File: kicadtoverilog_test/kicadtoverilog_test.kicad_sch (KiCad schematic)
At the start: 3 parts, among them X1 DGOF5S3

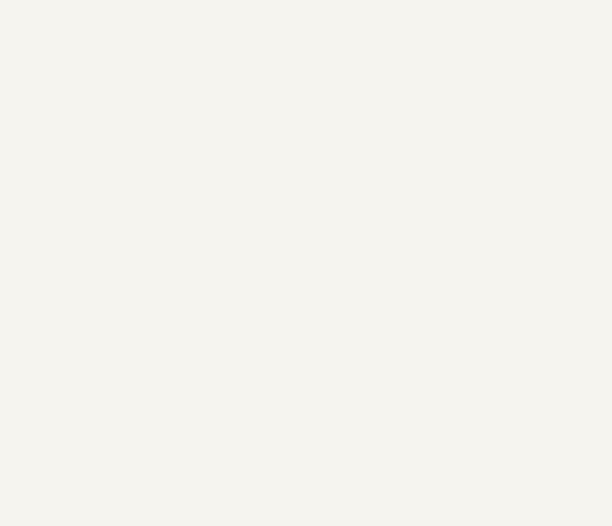
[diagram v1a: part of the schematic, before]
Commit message: Switch to KiCad 6.0 release
Use Command line args with argparse
Add some docs
Copy over synthesis_defs.v to verilog directory during run
Regularize logging
Fix bug with single nets on two module pins (Use wire statements for all nets, with assign statements for each module pin.)
Add test block with big divby3 from Atari TIA chip
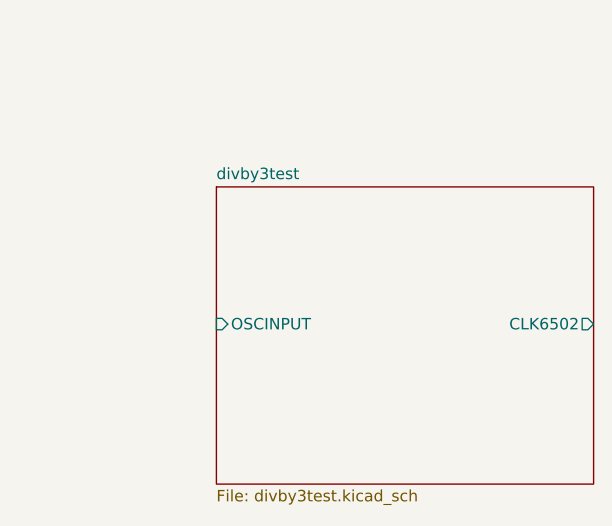
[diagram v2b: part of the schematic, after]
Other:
- added sheet divby3test (divby3test.kicad_sch)
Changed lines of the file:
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@@
 (kicad_sch (version 20211123) (generator eeschema)
-  (paper "A4")
+  (paper "USLetter")
   (wire (pts (xy 114.3 57.15) (xy 114.3 58.42))
     (stroke (width 0) (type default) (color 0 0 0 0))
@@
     (pin "1")
     (pin "2")
+  )
+  (sheet (at 96.52 106.68) (size 41.91 33.02) (fields_autoplaced)
+    (stroke (width 0.1524) (type solid) (color 0 0 0 0))
+    (fill (color 0 0 0 0.0000))
+    (property "Sheet name" "divby3test" (id 0) (at 96.52 105.9684 0)
+      (effects (font (size 1.27 1.27)) (justify left bottom))
+    )
+    (property "Sheet file" "divby3test.kicad_sch" (id 1) (at 96.52 140.2846 0)
+      (effects (font (size 1.27 1.27)) (justify left top))
+    )
+    (pin "CLK6502" output (at 138.43 121.92 0)
+      (effects (font (size 1.27 1.27)) (justify right))
+    )
+    (pin "OSCINPUT" input (at 96.52 121.92 180)
+      (effects (font (size 1.27 1.27)) (justify left))
+    )
   )
   (sheet (at 67.31 49.53) (size 25.4 27.94) (fields_autoplaced)
@@
     (path "/4f2d6a8d-0e80-4d54-bbae-408c1fcd4a62/633f75c5-3e59-4c5c-acaa-7b07045091db" (page "3"))
     (path "/4f2d6a8d-0e80-4d54-bbae-408c1fcd4a62/f15199f8-d839-4b26-a88d-cbb37c25a286" (page "4"))
+    (path "/1ee9928d-39f3-49de-bfea-81da4b94202b" (page "5"))
   )
   (symbol_instances
@@
       (reference "U4") (unit 1) (value "NOT") (footprint "")
     )
+    (path "/1ee9928d-39f3-49de-bfea-81da4b94202b/de77cc3b-6461-4584-bece-1b82a64083cf"
+      (reference "U5") (unit 1) (value "NOR2") (footprint "")
+    )
+    (path "/1ee9928d-39f3-49de-bfea-81da4b94202b/7a863598-1fe4-4965-ab0e-1f5f7c693cce"
+      (reference "U6") (unit 1) (value "NOR2") (footprint "")
+    )
+    (path "/1ee9928d-39f3-49de-bfea-81da4b94202b/aa8b3dd5-a5db-4d28-9f06-c334420f0ab0"
+      (reference "U7") (unit 1) (value "NOR2") (footprint "")
+    )
+    (path "/1ee9928d-39f3-49de-bfea-81da4b94202b/067be3a4-5e77-4472-9815-f50aab9fa6e2"
+      (reference "U8") (unit 1) (value "NOR2") (footprint "")
+    )
+    (path "/1ee9928d-39f3-49de-bfea-81da4b94202b/2800f70a-c288-469b-9829-771526ce2d9e"
+      (reference "U9") (unit 1) (value "NOR2") (footprint "")
+    )
+    (path "/1ee9928d-39f3-49de-bfea-81da4b94202b/cd372e86-2860-41ec-9d38-36aaf34b5770"
+      (reference "U10") (unit 1) (value "AND2") (footprint "")
+    )
+    (path "/1ee9928d-39f3-49de-bfea-81da4b94202b/b0d9aeee-3dba-4aa3-a75e-a4ba0c4a286b"
+      (reference "U11") (unit 1) (value "AND2") (footprint "")
+    )
+    (path "/1ee9928d-39f3-49de-bfea-81da4b94202b/887bada7-fc95-4e33-a94c-ef38c1958dfe"
+      (reference "U12") (unit 1) (value "NOR2") (footprint "")
+    )
+    (path "/1ee9928d-39f3-49de-bfea-81da4b94202b/856303fa-24c8-41cb-88b2-1f106ae8656c"
+      (reference "U13") (unit 1) (value "NOR2") (footprint "")
+    )
+    (path "/1ee9928d-39f3-49de-bfea-81da4b94202b/20582dd1-49d6-455e-9246-f48e6caa6db7"
+      (reference "U14") (unit 1) (value "NOR2") (footprint "")
+    )
+    (path "/1ee9928d-39f3-49de-bfea-81da4b94202b/b4166ee3-09bf-48a7-8d74-8969bd6d2dd3"
+      (reference "U15") (unit 1) (value "NOT") (footprint "")
+    )
+    (path "/1ee9928d-39f3-49de-bfea-81da4b94202b/6c620b1f-3b68-45a2-afba-bbd859b22d82"
+      (reference "U16") (unit 1) (value "NOR2") (footprint "")
+    )
+    (path "/1ee9928d-39f3-49de-bfea-81da4b94202b/d6840884-81c4-4835-9a07-0471b17aca9d"
+      (reference "U17") (unit 1) (value "NOR2") (footprint "")
+    )
+    (path "/1ee9928d-39f3-49de-bfea-81da4b94202b/02ecf064-5973-4753-9e25-8af2823609b1"
+      (reference "U18") (unit 1) (value "NOR2") (footprint "")
+    )
+    (path "/1ee9928d-39f3-49de-bfea-81da4b94202b/3af2825f-8ffc-4a6a-be03-a0adf47385f2"
+      (reference "U19") (unit 1) (value "NOR2") (footprint "")
+    )
+    (path "/1ee9928d-39f3-49de-bfea-81da4b94202b/5f9c655e-4dae-40a5-ae38-5294b8242232"
+      (reference "U20") (unit 1) (value "AND2") (footprint "")
+    )
+    (path "/1ee9928d-39f3-49de-bfea-81da4b94202b/9912dfed-5efa-49d5-99d4-7fa8c479d8d9"
+      (reference "U21") (unit 1) (value "AND2") (footprint "")
+    )
+    (path "/1ee9928d-39f3-49de-bfea-81da4b94202b/fee1bc3c-60fe-45a5-8fef-c8b543d31634"
+      (reference "U22") (unit 1) (value "NOR2") (footprint "")
+    )
+    (path "/1ee9928d-39f3-49de-bfea-81da4b94202b/8afc546e-224a-45b0-a565-0c848fec0069"
+      (reference "U23") (unit 1) (value "NOR2") (footprint "")
+    )
     (path "/844f01a0-ac23-4a99-910e-4e91c579bb2b"
